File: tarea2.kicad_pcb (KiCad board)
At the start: 4 copper layers, 37 x 39 mm, 19 parts, among them IC1 LDO40LPURY, J1 Conn_01x02_Pin, J2 BUS I2C, J3 Conn_01x07, J4 USB_C_Receptacle_USB2.0_16P, U1 STM32G030K8Tx, U2 CH340N

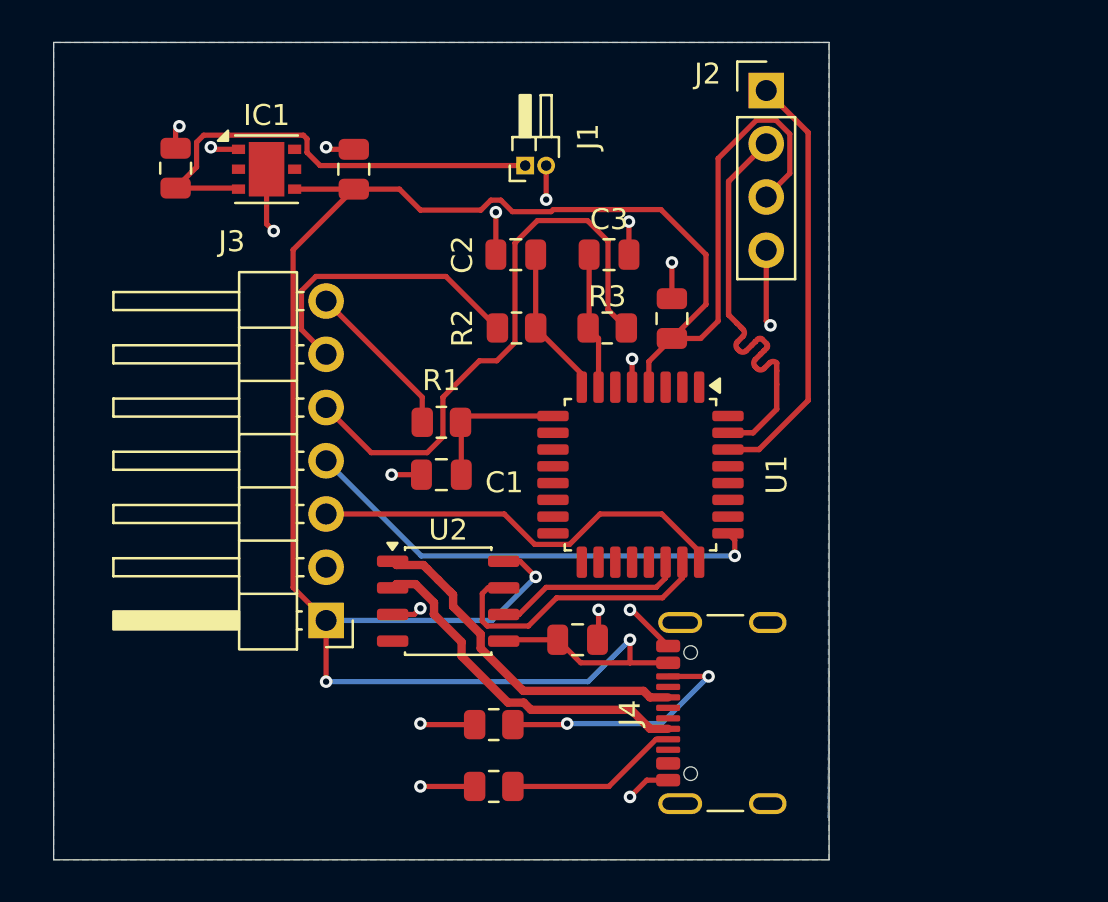
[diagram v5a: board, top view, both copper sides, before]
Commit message: Se ha raelizado la corrección de posición de la placa pero se han encontrado varios errores que dificcultan el enrutado y finalización de la placa.
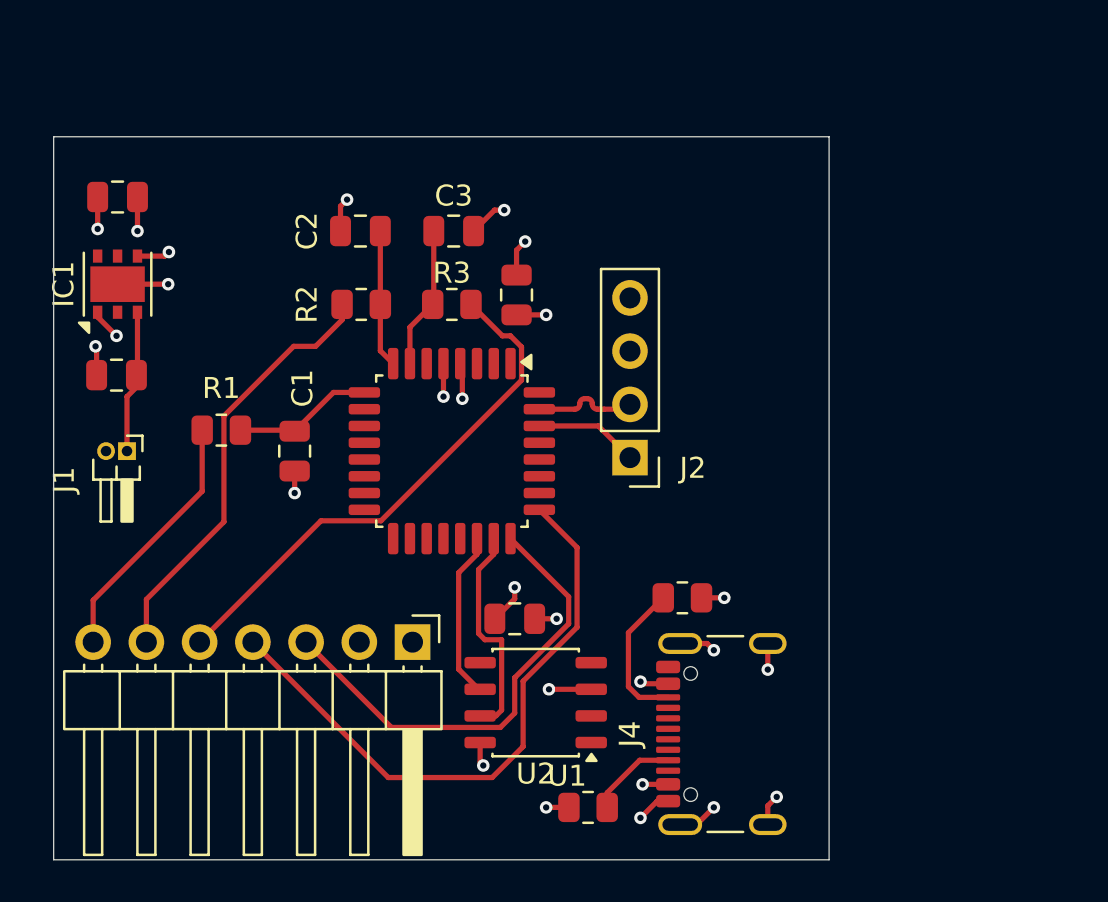
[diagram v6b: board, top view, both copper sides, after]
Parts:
- moved J1 23.4 mm to (137.0, 118.0), turned to -90 degrees
- moved J2 18.7 mm to (161.0, 118.3), turned to 180 degrees
- moved C4(desacople)3 11.3 mm to (136.6, 105.9), turned to 180 degrees
- moved R4 10.8 mm to (163.5, 125.0), turned to 180 degrees
- moved R1 10.5 mm to (141.5, 117.0)
- moved C4(desacople)2 10.3 mm to (136.5, 114.4), turned to 180 degrees
- moved U1 9.07 mm to (152.5, 118.0)
- moved IC1 8.98 mm to (136.6, 110.0), turned to 90 degrees
- moved C2 7.50 mm to (148.1, 107.5)
- moved C3 7.50 mm to (152.6, 107.5)
- moved C4(desacople)1 7.50 mm to (155.6, 110.5)
- moved R2 7.50 mm to (148.2, 111.0)
- moved R3 7.50 mm to (152.5, 111.0)
- moved C1 7.09 mm to (145.0, 118.0), turned to -90 degrees
- moved U2 6.39 mm to (156.5, 130.0), turned to 180 degrees
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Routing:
- net /Alimentación/VDD: track 110.8 -> 12.1 mm, vias 3 -> 8
- net USB_D-: track 16.8 -> 0.00 mm
- net USB_D+: track 16.6 -> 0.00 mm
- net Net-(IC1-VIN): track 22.4 -> 6.83 mm
- net Net-(J2-Pin_1): track 20.4 -> 4.95 mm
- net Net-(J2-Pin_2): track 20.3 -> 4.98 mm
- net Net-(J3-Pin_4): track 22.6 -> 29.7 mm, vias 1 -> 0
- net Net-(J3-Pin_6): track 14.2 -> 20.6 mm
- net Net-(J4-CC2): track 12.2 -> 7.03 mm, vias 2 -> 0
- net /Alimentación/GND: track 33.7 -> 28.7 mm, vias 17 -> 18
- net Net-(J3-Pin_7): track 7.69 -> 12.3 mm
- net Net-(J4-CC1): track 8.34 -> 4.25 mm
- net Net-(U1-PA10/PA12): track 13.8 -> 10.5 mm
- net Net-(J3-Pin_3): track 20.3 -> 23.0 mm
- net Net-(J3-Pin_5): track 27.7 -> 25.4 mm
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- added copper zone on In1.Cu, net /Alimentación/GND
- added copper zone on In2.Cu, net /Alimentación/VDD
- removed copper zone on B.Cu, net /Alimentación/GND
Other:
- board size 37 x 39 mm -> 37 x 34.5 mm

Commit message: Mejorar DRC
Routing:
- net /Alimentación/GND: track 28.7 -> 25.9 mm, vias 18 -> 16
- net /Alimentación/VDD: track 12.1 -> 12.5 mm, vias 8 -> 9
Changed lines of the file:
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@@
-	)
-	(segment
-		(start 155.5 125.05)
-		(end 155.5 124.5)
-		(width 0.25)
-		(layer "F.Cu")
-		(net "/Alimentación/VDD")
 	)
 	(segment
@@
 	)
 	(segment
-		(start 154.55 126)
-		(end 155.5 125.05)
+		(start 154.5 125.95)
+		(end 154.55 126)
+		(width 0.25)
+		(layer "F.Cu")
+		(net "/Alimentación/VDD")
+	)
+	(segment
+		(start 153.85 128.095)
+		(end 153.5 127.745)
 		(width 0.25)
 		(layer "F.Cu")
@@
 	)
 	(segment
+		(start 153.5 127.745)
+		(end 153.5 127.5)
+		(width 0.25)
+		(layer "F.Cu")
+		(net "/Alimentación/VDD")
+	)
+	(segment
+		(start 154.5 124.5)
+		(end 154.5 125.95)
+		(width 0.25)
+		(layer "F.Cu")
+		(net "/Alimentación/VDD")
+	)
+	(segment
 		(start 138.805 108.695)
 		(end 139 108.5)
@@
 	)
 	(via
-		(at 155.5 124.5)
+		(at 154.5 124.5)
 		(size 0.6)
 		(drill 0.3)
@@
 	(via
 		(at 161.5 129)
+		(size 0.6)
+		(drill 0.3)
+		(layers "F.Cu" "B.Cu")
+		(net "/Alimentación/VDD")
+	)
+	(via
+		(at 153.5 127.5)
 		(size 0.6)
 		(drill 0.3)
@@
 	)
 	(segment
-		(start 164.18 135.82)
-		(end 165 135)
+		(start 161.7 134.7)
+		(end 161.5 134.5)
+		(width 0.25)
+		(layer "F.Cu")
+		(net "/Alimentación/GND")
+	)
+	(segment
+		(start 162.82 128.3)
+		(end 161.8 128.3)
 		(width 0.25)
 		(layer "F.Cu")
@@
 	)
 	(segment
-		(start 167.575 134.925)
-		(end 168 134.5)
-		(width 0.25)
-		(layer "F.Cu")
-		(net "/Alimentación/GND")
-	)
-	(segment
 		(start 147.1875 106.3125)
 		(end 147.5 106)
@@
 	)
 	(segment
-		(start 167.575 135.82)
-		(end 167.575 134.925)
-		(width 0.25)
-		(layer "F.Cu")
-		(net "/Alimentación/GND")
-	)
-	(segment
 		(start 135.55 113.05)
 		(end 135.5 113)
@@
 	)
 	(segment
-		(start 163.395 127.18)
-		(end 164.68 127.18)
-		(width 0.25)
-		(layer "F.Cu")
-		(net "/Alimentación/GND")
-	)
-	(segment
 		(start 162.82 134.7)
 		(end 162.3 134.7)
@@
 	)
 	(segment
+		(start 161.4767 134.5233)
+		(end 161.4767 134.639798)
+		(width 0.25)
+		(layer "F.Cu")
+		(net "/Alimentación/GND")
+	)
+	(segment
 		(start 147.1875 107.5)
 		(end 147.1875 106.3125)
@@
 	)
 	(segment
+		(start 161.8 128.3)
+		(end 161.5 128)
+		(width 0.25)
+		(layer "F.Cu")
+		(net "/Alimentación/GND")
+	)
+	(segment
 		(start 164.4125 125)
 		(end 165.5 125)
@@
 	)
 	(segment
-		(start 167.575 127.18)
-		(end 167.575 128.425)
-		(width 0.25)
-		(layer "F.Cu")
-		(net "/Alimentación/GND")
-	)
-	(segment
 		(start 139 110)
 		(end 138.965 110.035)
@@
 	)
 	(segment
-		(start 167.5 128.5)
-		(end 167.575 128.425)
-		(width 0.25)
-		(layer "F.Cu")
-		(net "/Alimentación/GND")
-	)
-	(segment
 		(start 135.6 105.875)
 		(end 135.6 107.4)
@@
 	)
 	(segment
-		(start 164.68 127.18)
-		(end 165 127.5)
+		(start 161.5 134.5)
+		(end 161.4767 134.5233)
 		(width 0.25)
 		(layer "F.Cu")
@@
 		(net "/Alimentación/GND")
 	)
+	(segment
+		(start 162.82 134.7)
+		(end 161.7 134.7)
+		(width 0.25)
+		(layer "F.Cu")
+		(net "/Alimentación/GND")
+	)
 	(via
 		(at 155 106.5)
@@
 	)
 	(via
-		(at 168 134.5)
-		(size 0.6)
-		(drill 0.3)
-		(layers "F.Cu" "B.Cu")
-		(net "/Alimentación/GND")
-	)
-	(via
 		(at 165.5 125)
 		(size 0.6)
@@
 	)
 	(via
+		(at 161.5 128)
+		(size 0.6)
+		(drill 0.3)
+		(layers "F.Cu" "B.Cu")
+		(net "/Alimentación/GND")
+	)
+	(via
 		(at 136.5 112.5)
 		(size 0.6)
@@
 	)
 	(via
-		(at 167.575 128.425)
-		(size 0.6)
-		(drill 0.3)
-		(layers "F.Cu" "B.Cu")
-		(net "/Alimentación/GND")
-	)
-	(via
-		(at 165 135)
-		(size 0.6)
-		(drill 0.3)
-		(layers "F.Cu" "B.Cu")
-		(net "/Alimentación/GND")
-	)
-	(via
 		(at 157.5 126)
 		(size 0.6)
@@
 	)
 	(via
-		(at 165 127.5)
-		(size 0.6)
-		(drill 0.3)
+		(at 161.4767 134.639798)
+		(size 0.6)
+		(drill 0.3)
